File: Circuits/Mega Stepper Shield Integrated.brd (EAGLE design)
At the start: 110.5 x 80 mm, 70 parts, among them IC1 MC33269ST-5.0T3, IC2 MC33269D-5.0, IC3 ATMEGA2560-16AU, IC4 ATMEGA8U2-MU, IC5 LM358D, IC6 LP2985-33DBVR, Q2 16MHz, T1 2N2222, T2 FDN340P, X1 057-040-1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

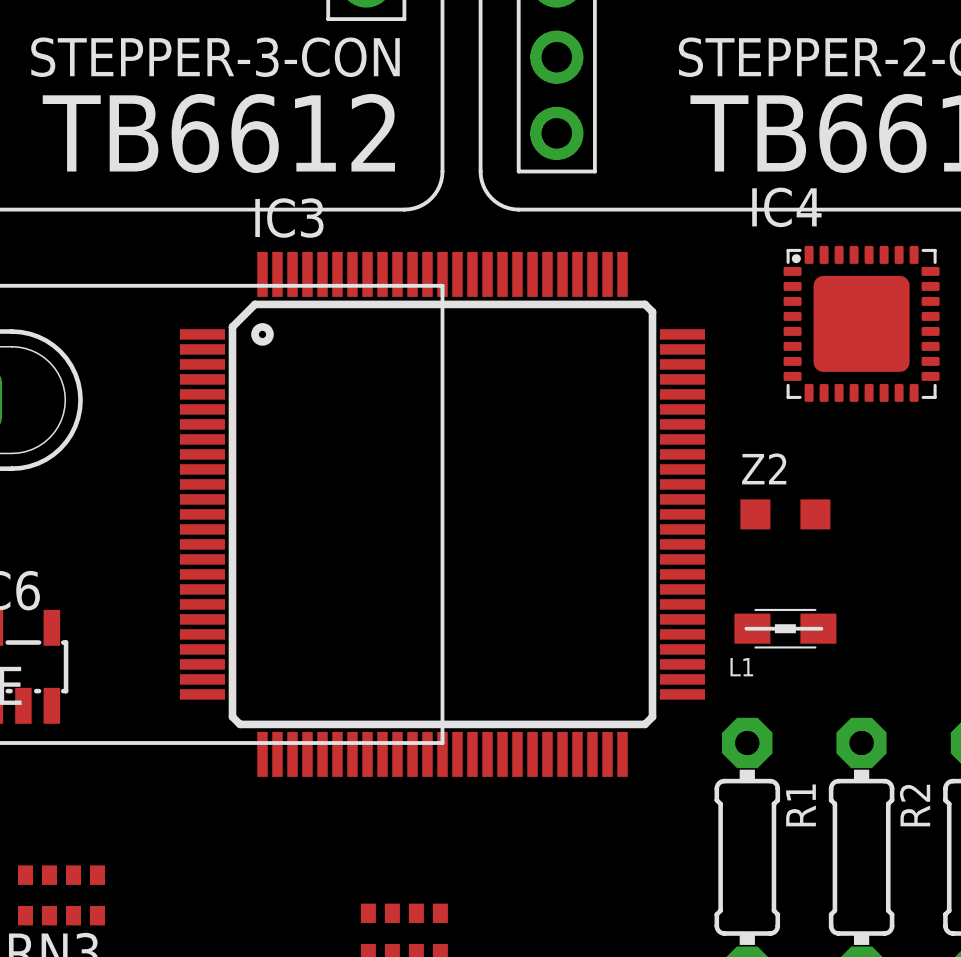
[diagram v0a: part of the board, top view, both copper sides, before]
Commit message: Create Integrated Version of Board
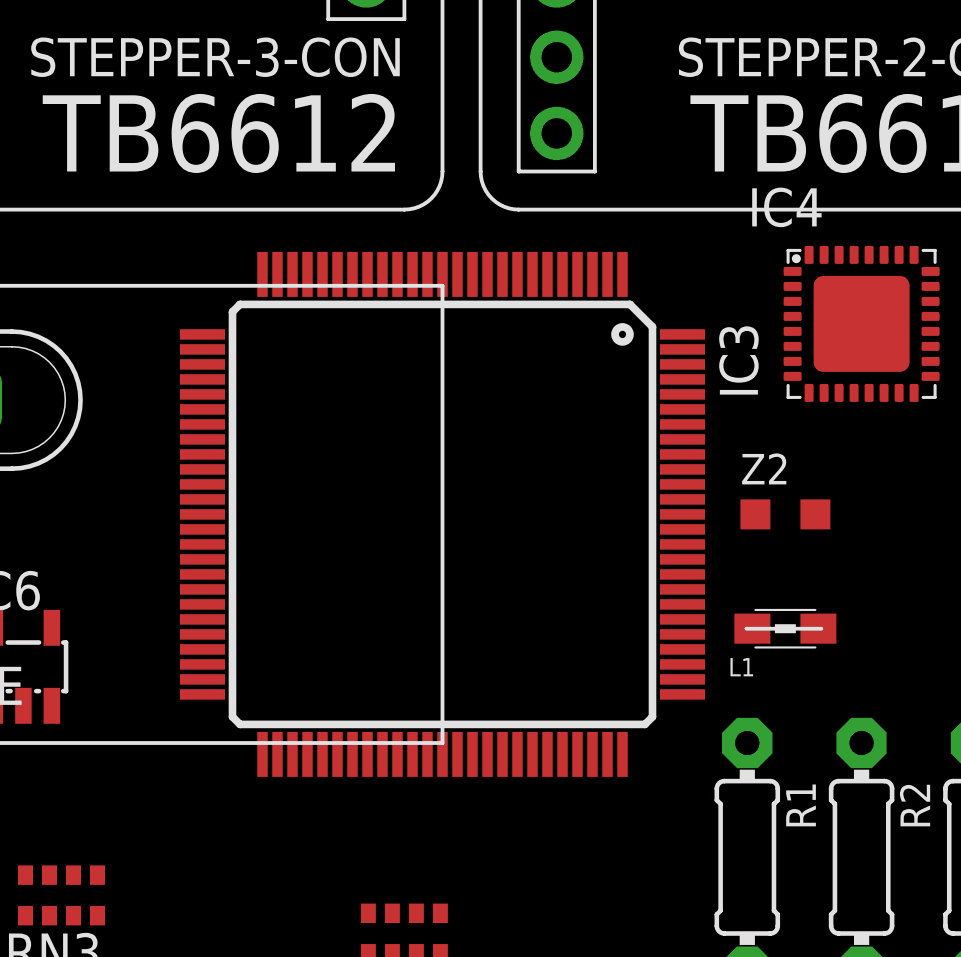
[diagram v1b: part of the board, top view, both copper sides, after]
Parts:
- turned IC3 to 270 degrees
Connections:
- removed net N$50: X1.22
- removed net N$51: X1.24
- removed net N$52: X1.26
- removed net N$53: X1.28
- removed net N$56: X1.30
- removed net N$57: X1.32
- removed net N$58: X1.34
- removed net N$59: X1.36
- removed net N$60: X1.38
- removed net N$61: X1.40
- net 40: now also X1.22
- net 41: now also X1.24
- net 42: now also X1.26
- net 43: now also X1.28
- net 44: now also X1.30
- net 45: now also X1.32
- net 46: now also X1.34
- net 47: now also X1.36
- net 48: now also X1.38
- net 49: now also X1.40
